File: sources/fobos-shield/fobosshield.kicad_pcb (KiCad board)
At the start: 2 copper layers, 83.8 x 63.5 mm, 154 parts, among them J1 Target, J10 ADCin, J11 PP1, J12 PP2, J13 Clock, J14 Trigger, J15 CSM5VCur, J16 Conn_01x01, J17 Barrel_Jack_Switch, J18 Conn_01x02, J19 Conn_01x02, J2 Glitch, J20 CSM3V3Cur, J21 GND, J22 GND, J3 Analog, J4 IOH, J5 SPI, J6 Analog2, J7 Power, J8 IOL, J9 SPI2, Q1 IRF7807Z, Q2 IRLML2502, Q3 BSS138L, U1 RB-0509D, U10 INA225, U11 INA225, U12 LD1117S33TR_SOT223, U2 REE-0505S, U3 LM317L_SO8, U4 LM337L_SO8, U5 LD59015, U6 LP3985IM5-3.0, U7 AD8331, U8 TPS7A7100_VQFN20, U9 AD9215

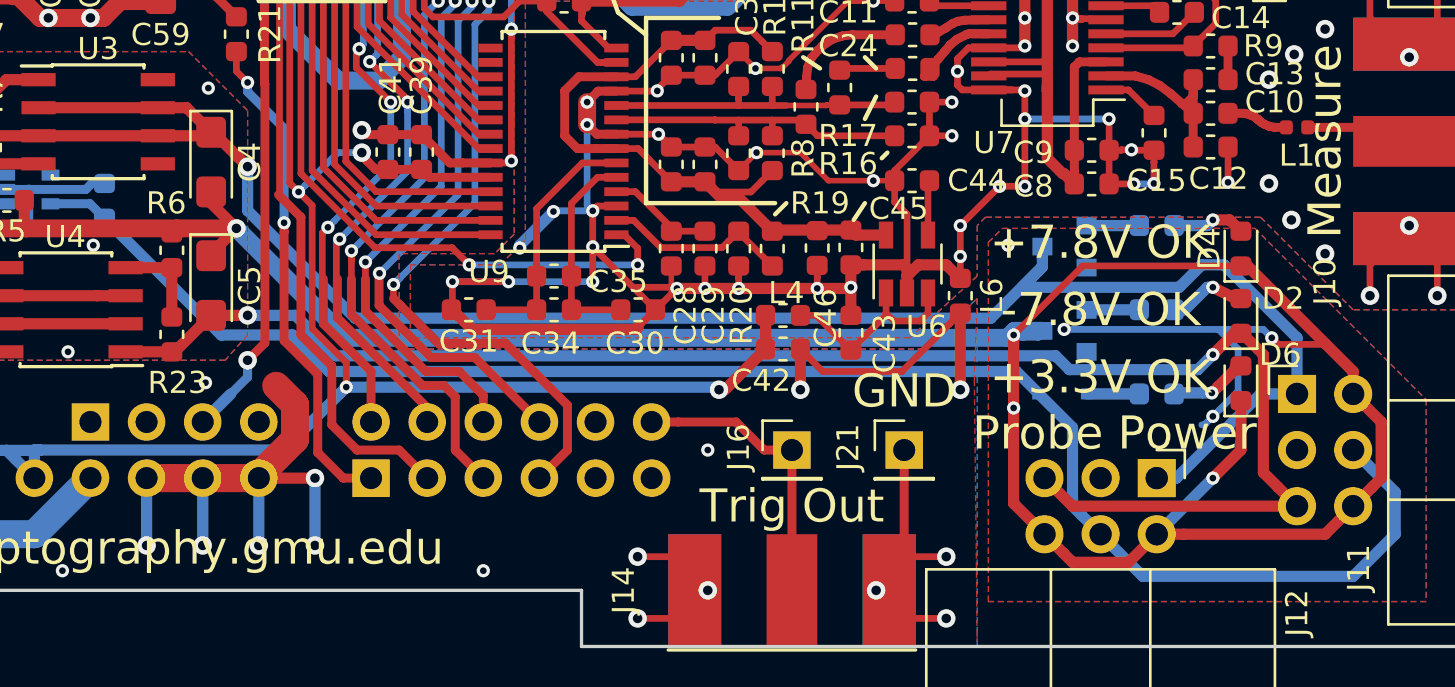
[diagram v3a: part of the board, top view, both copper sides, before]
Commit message: added more FPGA pins and fixed bug in FOBOS shield
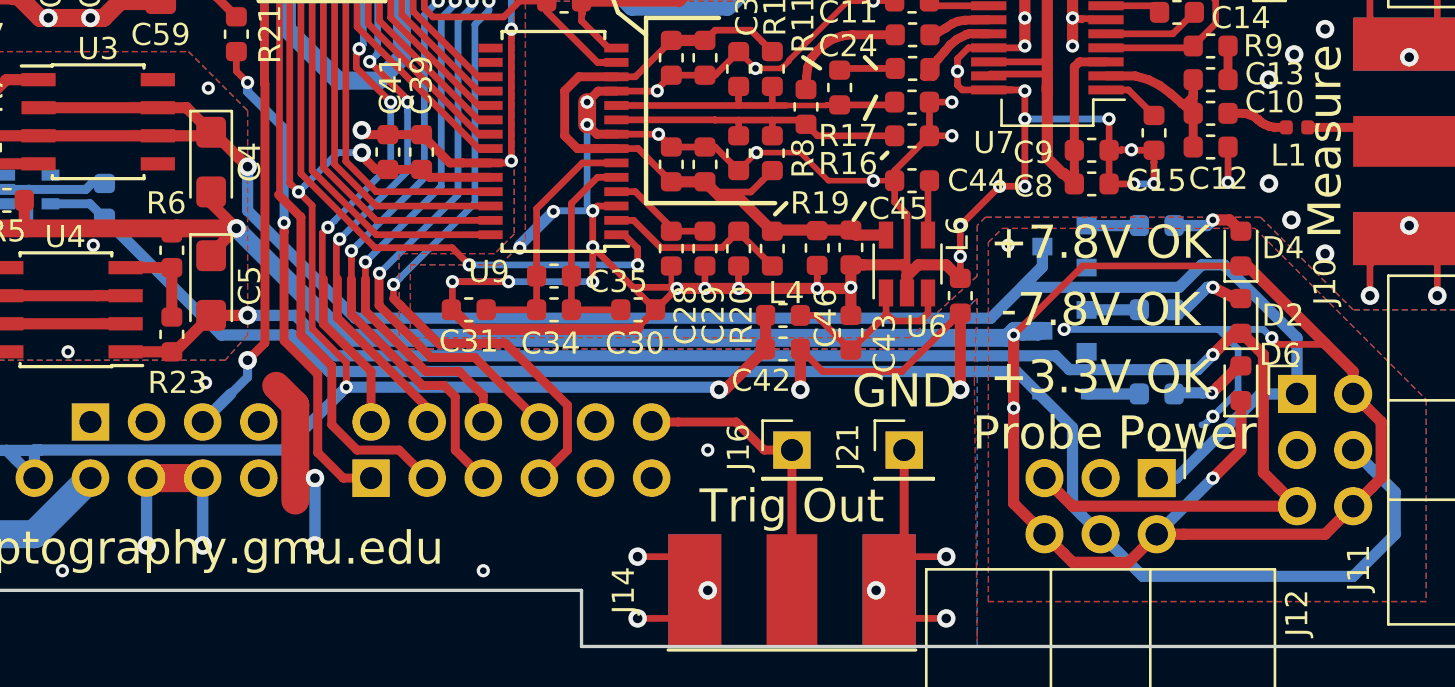
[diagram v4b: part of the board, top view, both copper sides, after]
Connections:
- J7 pad 8: GND -> VU_CK
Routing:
- net GND: track 561.3 -> 553.6 mm, vias 118 -> 117

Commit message: some modifications to the shield
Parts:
- added H1: 573100D00010G, cerg:573100D00010G, F.Cu at (66.0, 39.4)
- C51, C52: footprint Capacitor_SMD:C_0603_1608Metric -> Capacitor_SMD:C_0402_1005Metric
- D8: value 2V4 -> 3V9
- R27: value 100R -> 330R
- R33: value 470R -> 330R

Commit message: forgot
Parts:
- moved H1 29.6 mm to (44.5, 19.1)
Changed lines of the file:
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@@
   )
   (module cerg:573100D00010G (layer F.Cu)
-    (at 66.04 39.37)
+    (at 44.45 19.05)
     (descr 573100D00010G-1)
     (tags Hardware)

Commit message: trying new locations of components on shield
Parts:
- added D13: 1N4148, Diode_SMD:D_SOD-323F, F.Cu at (5.08, 44.5)
- R33: value 330R -> 100R
- moved D1 100.4 mm to (7.25, 100.0)
- moved D2 100.4 mm to (15.2, 103.1)
- moved D3 100.4 mm to (7.15, 106.7)
- moved D4 100.4 mm to (15.2, 100.1)
- moved D5 100.4 mm to (7.25, 103.8)
- moved D6 100.4 mm to (15.2, 106.2)
- moved J11 100.4 mm to (17.8, 106.7)
- moved J12 100.4 mm to (11.4, 110.5)
- moved R24 100.4 mm to (11.4, 99.1)
- moved R25 100.4 mm to (11.4, 102.9)
- moved R26 100.4 mm to (11.4, 106.7)
- moved Q1 82.6 mm to (184.8, 35.6)
- moved Q2 82.6 mm to (186.2, 34.3)
- moved R2 82.6 mm to (179.1, 36.8)
- moved J13 82.6 mm to (172.7, 27.9)
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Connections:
- J4 pad 1: ADC_D5 -> CW_SCK
- J4 pad 16: ADC_CLK -> CW_HS1
- J4 pad 2: ADC_D6 -> CW_TARG2
- J4 pad 3: ADC_D7 -> CW_MOSI
- J4 pad 4: ADC_D8 -> CW_TARG1
- J4 pad 5: ADC_D9 -> CW_MISO
- J4 pad 6: ADC_OR -> CW_RST
- J8 pad 1: CW_RST -> ADC_D1
- J8 pad 10: CW_TARG4 -> ADC_D7
- J8 pad 11: CW_PDID -> ADC_OR
- J8 pad 12: ADC_D0 -> ADC_D9
- J8 pad 13: ADC_D1 -> CW_PDID
- J8 pad 14: ADC_D2 -> CW_TARG4
- J8 pad 15: ADC_D3 -> CW_PDIC
- J8 pad 16: ADC_D4 -> CW_TARG3
- J8 pad 2: CW_MISO -> ADC_D0
- J8 pad 3: CW_TARG1 -> ADC_D3
- J8 pad 4: CW_MOSI -> ADC_D2
- J8 pad 5: CW_TARG2 -> ADC_D5
- J8 pad 6: CW_SCK -> ADC_D4
- J8 pad 7: CW_TARG3 -> ADC_D6
- J8 pad 8: CW_HS1 -> ADC_CLK
- J8 pad 9: CW_PDIC -> ADC_D8
- R33 pad 1: Net-(C58-Pad1) -> Net-(D13-Pad1)
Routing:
- net GND: track 553.6 -> 0.00 mm, vias 117 -> 1
- net GNDA: track 231.0 -> 0.00 mm, vias 66 -> 0
- net /Power/GNDP: track 181.3 -> 0.00 mm, vias 15 -> 0
- net IN: track 111.5 -> 0.00 mm
- net VCC5V0: track 110.2 -> 0.00 mm, vias 3 -> 0
- net CSM3V3: track 108.0 -> 0.00 mm, vias 2 -> 0
- net VCC3V3: track 103.1 -> 0.00 mm, vias 6 -> 0
- net /Power/+7V8P: track 88.7 -> 0.00 mm, vias 1 -> 0
- net /Power/3V3P: track 75.3 -> 0.00 mm
- net /Power/-7V8P: track 74.3 -> 0.00 mm, vias 2 -> 0
- net CSM5V: track 73.7 -> 0.00 mm, vias 1 -> 0
- net CW_HS2: track 72.5 -> 0.00 mm
- net ADC_CLK: track 69.5 -> 0.00 mm, vias 2 -> 0
- net ADC_OR: track 58.4 -> 0.00 mm, vias 2 -> 0
- net CW_HS1: track 52.4 -> 0.00 mm
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- removed copper zone on B.Cu, net GND
- removed copper zone on F.Cu, net GND
- removed copper zone on B.Cu, net GNDA
- removed copper zone on F.Cu, net GNDA
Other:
- board text added: "rev 2.0"
- board text removed: "rev 1.1"

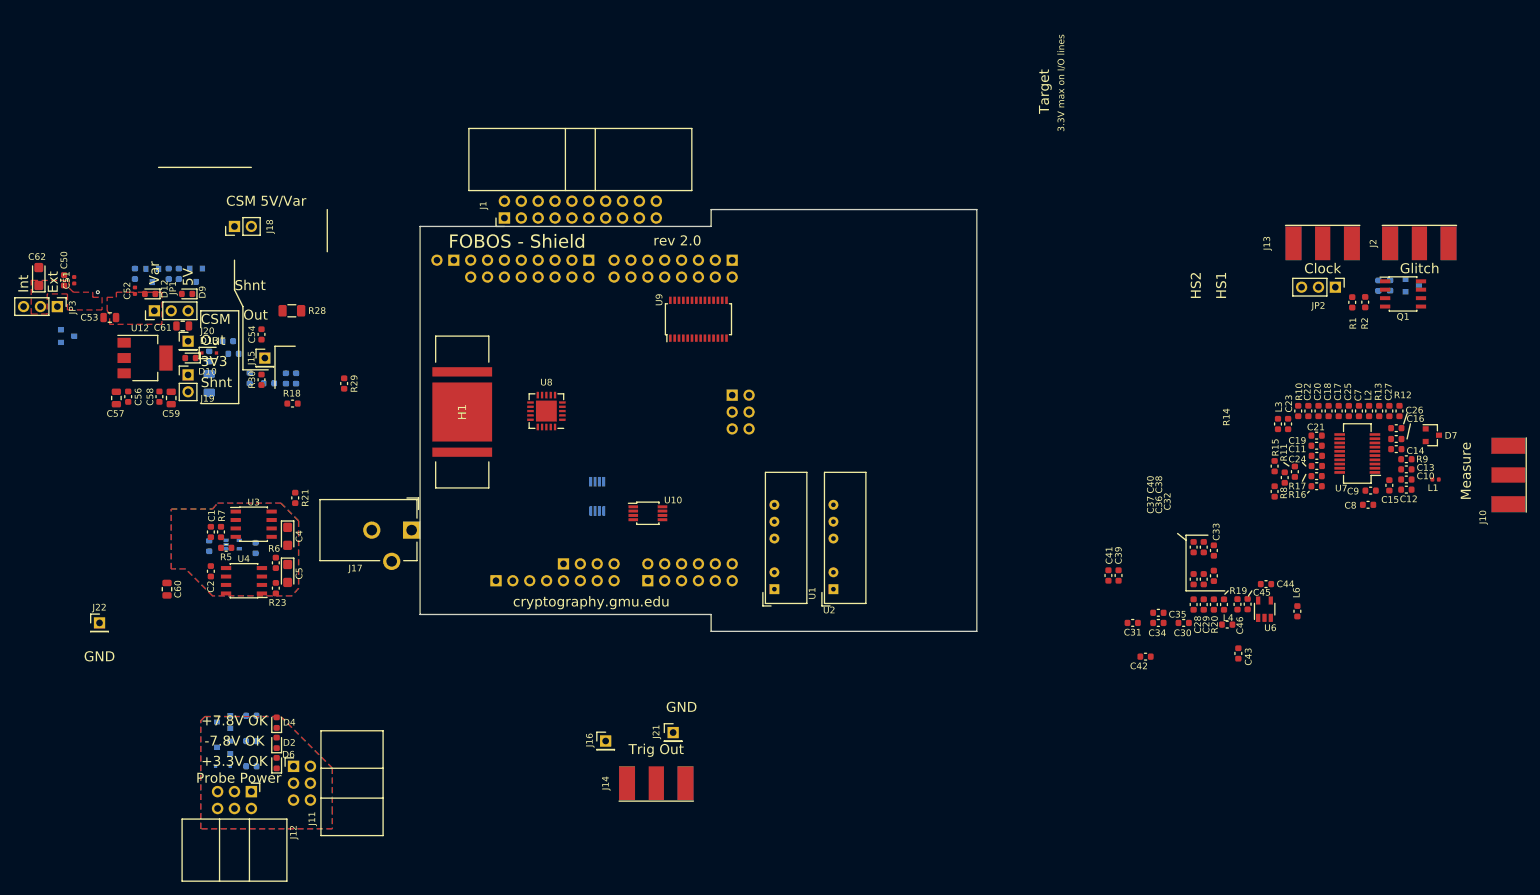
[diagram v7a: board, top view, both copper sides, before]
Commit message: started open ADC layout
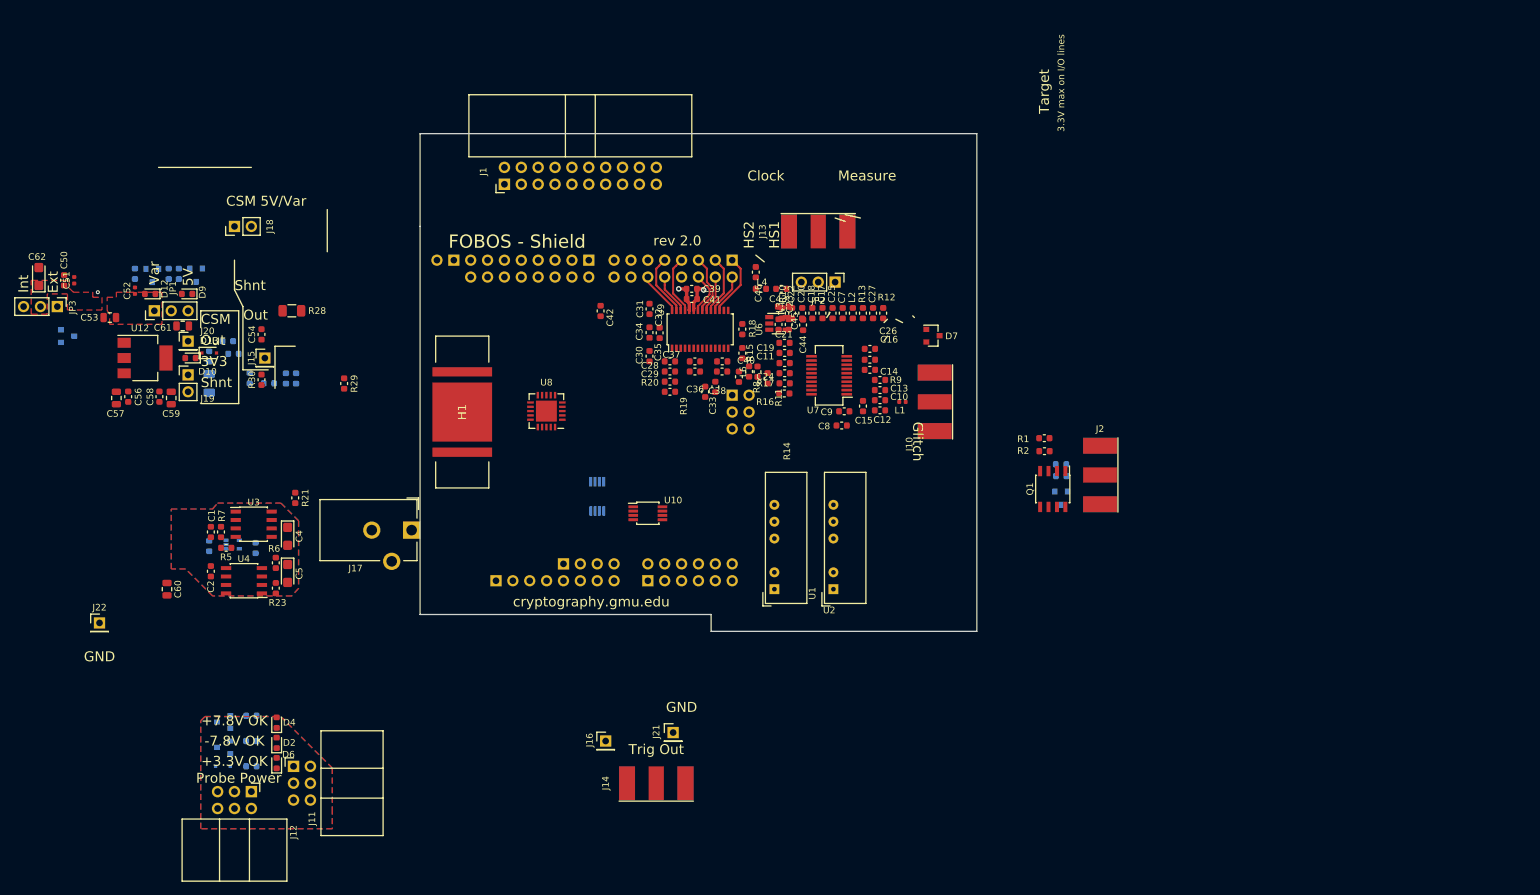
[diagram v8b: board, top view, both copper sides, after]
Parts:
- moved C42 97.2 mm to (64.0, 38.1), turned to 270 degrees
- moved L6 92.2 mm to (85.3, 44.5), turned to 90 degrees
- moved C30 89.9 mm to (71.4, 44.9), turned to 270 degrees
- moved R19 89.4 mm to (74.4, 50.3), turned to 0 degrees
- moved R20 88.5 mm to (74.4, 48.8), turned to 0 degrees
- moved C34 88.2 mm to (71.4, 41.4), turned to 270 degrees
- moved C46 88.1 mm to (87.4, 32.3)
- moved C43 88.0 mm to (91.2, 34.8), turned to 180 degrees
- moved C29 87.7 mm to (74.4, 47.2), turned to 0 degrees
- moved J10 87.1 mm to (114.3, 51.8)
- moved C28 86.9 mm to (74.4, 45.7), turned to 0 degrees
- moved C31 86.8 mm to (71.4, 37.8), turned to 90 degrees
- moved L4 86.5 mm to (88.1, 34.8)
- moved C35 86.1 mm to (72.9, 41.4), turned to 270 degrees
- moved U6 84.9 mm to (90.7, 40.0), turned to 0 degrees
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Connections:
- J8 pad 1: ADC_D1 -> ADC_D0
- J8 pad 2: ADC_D0 -> ADC_D1
- J8 pad 3: ADC_D3 -> ADC_D2
- J8 pad 4: ADC_D2 -> ADC_D3
- J8 pad 5: ADC_D5 -> ADC_D4
- J8 pad 6: ADC_D4 -> ADC_D5
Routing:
- net ADC_D0: track 0.00 -> 9.40 mm
- net ADC_D8: track 0.00 -> 9.34 mm
- net ADC_D4: track 0.00 -> 9.09 mm
- net ADC_D2: track 0.00 -> 8.89 mm
- net ADC_D6: track 0.00 -> 8.83 mm
- net ADC_D5: track 0.00 -> 7.00 mm
- net ADC_D9: track 0.00 -> 6.54 mm
- net ADC_D1: track 0.00 -> 6.08 mm
- net ADC_D7: track 0.00 -> 6.02 mm
- net ADC_D3: track 0.00 -> 5.68 mm
- net VCC3V3: track 0.00 -> 4.59 mm, vias 0 -> 1
- net GND: track 0.00 -> 4.56 mm, vias 1 -> 2
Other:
- board size 83.8 x 63.5 mm -> 83.8 x 74.9 mm
